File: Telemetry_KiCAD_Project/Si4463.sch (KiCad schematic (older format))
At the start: 16 parts

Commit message: Annotated Components
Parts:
- gave numbers to parts that had none: 16

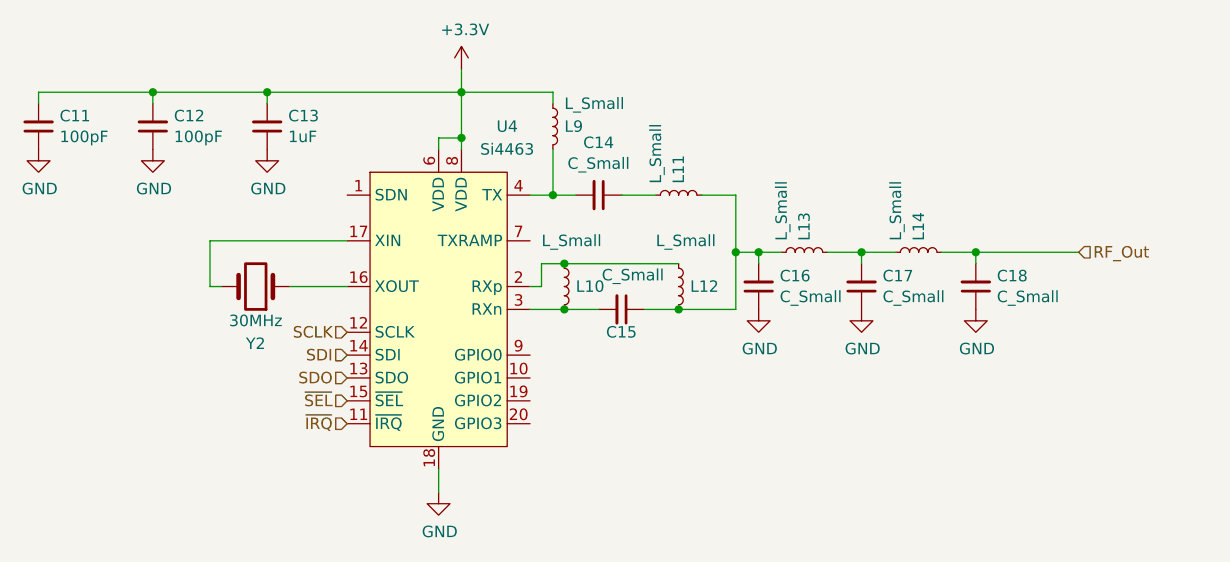
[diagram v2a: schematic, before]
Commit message: Corrected hierarchical pin directions, squashed bugs
There are still some warnings about pins being connected but not driven, don't know how to fix those at the moment
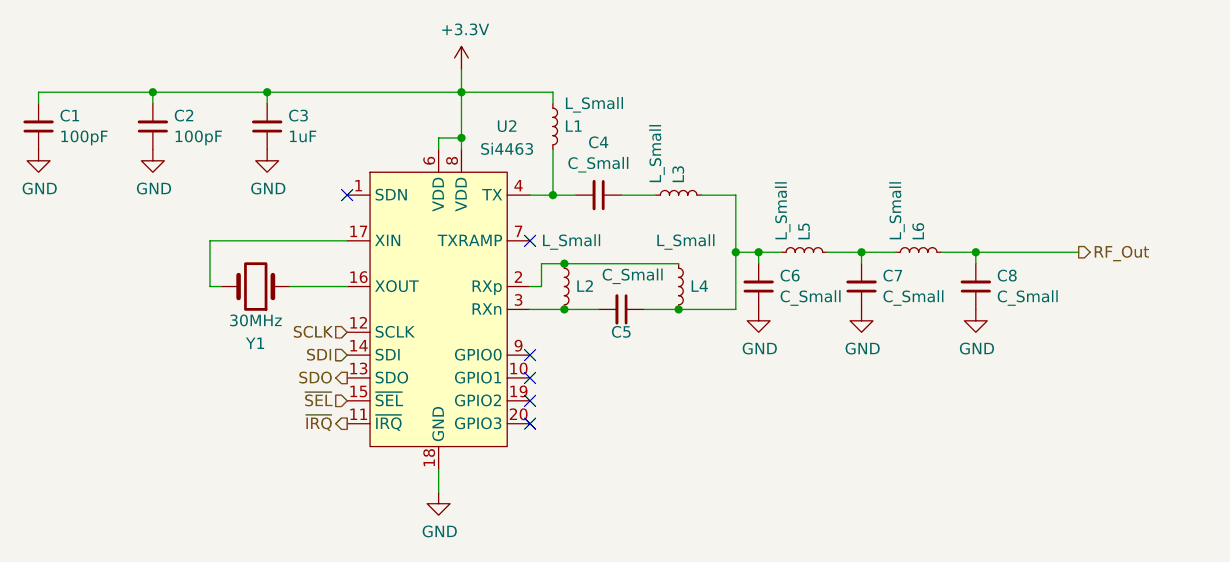
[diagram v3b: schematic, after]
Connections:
- no-connect marks 0 -> 6
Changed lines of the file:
@@
 AR Path="/619D9C89/619D9E16" Ref="U2"  Part="1"
 AR Path="/61A0416A/619D9E16" Ref="U4"  Part="1"
-F 0 "U4" H 6450 4450 50  0000 C CNN
+F 0 "U2" H 6450 4450 50  0000 C CNN
 F 1 "Si4463" H 6450 4350 50  0000 C CNN
 F 2 "Package_DFN_QFN:QFN-20-1EP_4x4mm_P0.5mm_EP2.6x2.6mm_ThermalVias" H 6150 4850 50  0001 C CNN
@@
 AR Path="/619D9C89/619DA640" Ref="C4"  Part="1"
 AR Path="/61A0416A/619DA640" Ref="C14"  Part="1"
-F 0 "C14" V 6621 3150 50  0000 C CNN
+F 0 "C4" V 6621 3150 50  0000 C CNN
 F 1 "C_Small" V 6712 3150 50  0000 C CNN
 F 2 "" H 6850 3150 50  0001 C CNN
@@
 Text HLabel 5750 4050 0    50   Input ~ 0
 ~SEL
-Text HLabel 5750 4150 0    50   Input ~ 0
+Text HLabel 5750 4150 0    50   Output ~ 0
 ~IRQ
-Text HLabel 5750 3950 0    50   Input ~ 0
+Text HLabel 5750 3950 0    50   Output ~ 0
 SDO
 Text HLabel 5750 3850 0    50   Input ~ 0
@@
 AR Path="/619D9C89/619DAC0C" Ref="Y1"  Part="1"
 AR Path="/61A0416A/619DAC0C" Ref="Y2"  Part="1"
-F 0 "Y2" H 5350 3800 50  0000 C CNN
+F 0 "Y1" H 5350 3800 50  0000 C CNN
 F 1 "30MHz" H 5350 3700 50  0000 C CNN
 F 2 "" H 5350 3550 50  0001 C CNN
@@
 AR Path="/619D9C89/619DA828" Ref="L2"  Part="1"
 AR Path="/61A0416A/619DA828" Ref="L10"  Part="1"
-F 0 "L10" H 6750 3550 50  0000 L CNN
+F 0 "L2" H 6750 3550 50  0000 L CNN
 F 1 "L_Small" H 6600 3750 50  0000 L CNN
 F 2 "" H 6700 3550 50  0001 C CNN
@@
 AR Path="/619D9C89/619E6B72" Ref="L3"  Part="1"
 AR Path="/61A0416A/619E6B72" Ref="L11"  Part="1"
-F 0 "L11" H 7250 3150 50  0000 L CNN
+F 0 "L3" H 7250 3150 50  0000 L CNN
 F 1 "L_Small" H 7250 3250 50  0000 L CNN
 F 2 "" H 7200 3150 50  0001 C CNN
@@
 AR Path="/619D9C89/619E8DE5" Ref="C5"  Part="1"
 AR Path="/61A0416A/619E8DE5" Ref="C15"  Part="1"
-F 0 "C15" V 7050 3650 50  0000 C CNN
+F 0 "C5" V 7050 3650 50  0000 C CNN
 F 1 "C_Small" V 6800 3700 50  0000 C CNN
 F 2 "" H 6950 3650 50  0001 C CNN
@@
 AR Path="/619D9C89/619EAA94" Ref="L4"  Part="1"
 AR Path="/61A0416A/619EAA94" Ref="L12"  Part="1"
-F 0 "L12" H 7250 3550 50  0000 L CNN
+F 0 "L4" H 7250 3550 50  0000 L CNN
 F 1 "L_Small" H 7100 3750 50  0000 L CNN
 F 2 "" H 7200 3550 50  0001 C CNN
@@
 AR Path="/619D9C89/619ECD33" Ref="C6"  Part="1"
 AR Path="/61A0416A/619ECD33" Ref="C16"  Part="1"
-F 0 "C16" H 7458 3504 50  0000 R CNN
+F 0 "C6" H 7458 3504 50  0000 R CNN
 F 1 "C_Small" H 7458 3595 50  0000 R CNN
 F 2 "" H 7550 3550 50  0001 C CNN
@@
 AR Path="/619D9C89/619F2EFE" Ref="L1"  Part="1"
 AR Path="/61A0416A/619F2EFE" Ref="L9"  Part="1"
-F 0 "L9" H 6700 2850 50  0000 L CNN
+F 0 "L1" H 6700 2850 50  0000 L CNN
 F 1 "L_Small" H 6700 2950 50  0000 L CNN
 F 2 "" H 6650 2850 50  0001 C CNN
@@
 AR Path="/619D9C89/619EE414" Ref="C8"  Part="1"
 AR Path="/61A0416A/619EE414" Ref="C18"  Part="1"
-F 0 "C18" H 8408 3504 50  0000 R CNN
+F 0 "C8" H 8408 3504 50  0000 R CNN
 F 1 "C_Small" H 8408 3595 50  0000 R CNN
 F 2 "" H 8500 3550 50  0001 C CNN
@@
 AR Path="/619D9C89/619EDC84" Ref="C7"  Part="1"
 AR Path="/61A0416A/619EDC84" Ref="C17"  Part="1"
-F 0 "C17" H 7908 3504 50  0000 R CNN
+F 0 "C7" H 7908 3504 50  0000 R CNN
 F 1 "C_Small" H 7908 3595 50  0000 R CNN
 F 2 "" H 8000 3550 50  0001 C CNN
@@
 AR Path="/619D9C89/619ECA9B" Ref="L6"  Part="1"
 AR Path="/61A0416A/619ECA9B" Ref="L14"  Part="1"
-F 0 "L14" H 8300 3400 50  0000 L CNN
+F 0 "L6" H 8300 3400 50  0000 L CNN
 F 1 "L_Small" H 8300 3500 50  0000 L CNN
 F 2 "" H 8250 3400 50  0001 C CNN
@@
 AR Path="/619D9C89/619EC46A" Ref="L5"  Part="1"
 AR Path="/61A0416A/619EC46A" Ref="L13"  Part="1"
-F 0 "L13" H 7800 3400 50  0000 L CNN
+F 0 "L5" H 7800 3400 50  0000 L CNN
 F 1 "L_Small" H 7800 3500 50  0000 L CNN
 F 2 "" H 7750 3400 50  0001 C CNN
@@
 AR Path="/619D9C89/619F7D57" Ref="C3"  Part="1"
 AR Path="/61A0416A/619F7D57" Ref="C13"  Part="1"
-F 0 "C13" H 5308 2804 50  0000 R CNN
+F 0 "C3" H 5308 2804 50  0000 R CNN
 F 1 "1uF" H 5308 2895 50  0000 R CNN
 F 2 "" H 5400 2850 50  0001 C CNN
@@
 AR Path="/619D9C89/619F860E" Ref="C2"  Part="1"
 AR Path="/61A0416A/619F860E" Ref="C12"  Part="1"
-F 0 "C12" H 4808 2804 50  0000 R CNN
+F 0 "C2" H 4808 2804 50  0000 R CNN
 F 1 "100pF" H 4808 2895 50  0000 R CNN
 F 2 "" H 4900 2850 50  0001 C CNN
@@
 AR Path="/619D9C89/619F8BD8" Ref="C1"  Part="1"
 AR Path="/61A0416A/619F8BD8" Ref="C11"  Part="1"
-F 0 "C11" H 4308 2804 50  0000 R CNN
+F 0 "C1" H 4308 2804 50  0000 R CNN
 F 1 "100pF" H 4308 2895 50  0000 R CNN
 F 2 "" H 4400 2850 50  0001 C CNN
@@
 Wire Wire Line
 	5400 2700 4900 2700
-Text HLabel 8950 3400 2    50   Input ~ 0
+Text HLabel 8950 3400 2    50   Output ~ 0
 RF_Out
+NoConn ~ 6550 3850
+NoConn ~ 6550 3950
+NoConn ~ 6550 4050
+NoConn ~ 6550 4150
+NoConn ~ 6550 3350
+NoConn ~ 5750 3150
 $EndSCHEMATC

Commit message: Assigned footprints to all components (except duplexer)
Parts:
- C1, C2, C3, C4, C5, C6, C7, C8: footprint (none) -> Capacitor_SMD:C_0603_1608Metric
- L1, L2, L3, L4, L5, L6: footprint (none) -> Inductor_SMD:L_0603_1608Metric
- Y1: footprint (none) -> Crystal:Crystal_SMD_0603-2Pin_6.0x3.5mm
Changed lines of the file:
@@
 F 0 "C4" V 6621 3150 50  0000 C CNN
 F 1 "C_Small" V 6712 3150 50  0000 C CNN
-F 2 "" H 6850 3150 50  0001 C CNN
+F 2 "Capacitor_SMD:C_0603_1608Metric" H 6850 3150 50  0001 C CNN
 F 3 "~" H 6850 3150 50  0001 C CNN
 	1    6850 3150
@@
 AR Path="/619D9C89/619DAEC1" Ref="#PWR0104"  Part="1"
 AR Path="/61A0416A/619DAEC1" Ref="#PWR0116"  Part="1"
-F 0 "#PWR0116" H 6150 4200 50  0001 C CNN
+F 0 "#PWR0104" H 6150 4200 50  0001 C CNN
 F 1 "GND" H 6155 4277 50  0000 C CNN
 F 2 "" H 6150 4450 50  0001 C CNN
@@
 AR Path="/619D9C89/619DB460" Ref="#PWR0105"  Part="1"
 AR Path="/61A0416A/619DB460" Ref="#PWR0117"  Part="1"
-F 0 "#PWR0117" H 6250 2450 50  0001 C CNN
+F 0 "#PWR0105" H 6250 2450 50  0001 C CNN
 F 1 "+3.3V" H 6265 2773 50  0000 C CNN
 F 2 "" H 6250 2600 50  0001 C CNN
@@
 F 0 "Y1" H 5350 3800 50  0000 C CNN
 F 1 "30MHz" H 5350 3700 50  0000 C CNN
-F 2 "" H 5350 3550 50  0001 C CNN
+F 2 "Crystal:Crystal_SMD_0603-2Pin_6.0x3.5mm" H 5350 3550 50  0001 C CNN
 F 3 "~" H 5350 3550 50  0001 C CNN
 	1    5350 3550
@@
 F 0 "L2" H 6750 3550 50  0000 L CNN
 F 1 "L_Small" H 6600 3750 50  0000 L CNN
-F 2 "" H 6700 3550 50  0001 C CNN
+F 2 "Inductor_SMD:L_0603_1608Metric" H 6700 3550 50  0001 C CNN
 F 3 "~" H 6700 3550 50  0001 C CNN
 	1    6700 3550
@@
 F 0 "L3" H 7250 3150 50  0000 L CNN
 F 1 "L_Small" H 7250 3250 50  0000 L CNN
-F 2 "" H 7200 3150 50  0001 C CNN
+F 2 "Inductor_SMD:L_0603_1608Metric" H 7200 3150 50  0001 C CNN
 F 3 "~" H 7200 3150 50  0001 C CNN
 	1    7200 3150
@@
 F 0 "C5" V 7050 3650 50  0000 C CNN
 F 1 "C_Small" V 6800 3700 50  0000 C CNN
-F 2 "" H 6950 3650 50  0001 C CNN
+F 2 "Capacitor_SMD:C_0603_1608Metric" H 6950 3650 50  0001 C CNN
 F 3 "~" H 6950 3650 50  0001 C CNN
 	1    6950 3650
@@
 F 0 "L4" H 7250 3550 50  0000 L CNN
 F 1 "L_Small" H 7100 3750 50  0000 L CNN
-F 2 "" H 7200 3550 50  0001 C CNN
+F 2 "Inductor_SMD:L_0603_1608Metric" H 7200 3550 50  0001 C CNN
 F 3 "~" H 7200 3550 50  0001 C CNN
 	1    7200 3550
@@
 F 0 "C6" H 7458 3504 50  0000 R CNN
 F 1 "C_Small" H 7458 3595 50  0000 R CNN
-F 2 "" H 7550 3550 50  0001 C CNN
+F 2 "Capacitor_SMD:C_0603_1608Metric" H 7550 3550 50  0001 C CNN
 F 3 "~" H 7550 3550 50  0001 C CNN
 	1    7550 3550
@@
 AR Path="/619D9C89/619F22FD" Ref="#PWR0106"  Part="1"
 AR Path="/61A0416A/619F22FD" Ref="#PWR0118"  Part="1"
-F 0 "#PWR0118" H 7550 3400 50  0001 C CNN
+F 0 "#PWR0106" H 7550 3400 50  0001 C CNN
 F 1 "GND" H 7555 3477 50  0000 C CNN
 F 2 "" H 7550 3650 50  0001 C CNN
@@
 F 0 "L1" H 6700 2850 50  0000 L CNN
 F 1 "L_Small" H 6700 2950 50  0000 L CNN
-F 2 "" H 6650 2850 50  0001 C CNN
+F 2 "Inductor_SMD:L_0603_1608Metric" H 6650 2850 50  0001 C CNN
 F 3 "~" H 6650 2850 50  0001 C CNN
 	1    6650 2850
@@
 AR Path="/619D9C89/619F1FAB" Ref="#PWR0107"  Part="1"
 AR Path="/61A0416A/619F1FAB" Ref="#PWR0119"  Part="1"
-F 0 "#PWR0119" H 8000 3400 50  0001 C CNN
+F 0 "#PWR0107" H 8000 3400 50  0001 C CNN
 F 1 "GND" H 8005 3477 50  0000 C CNN
 F 2 "" H 8000 3650 50  0001 C CNN
@@
 AR Path="/619D9C89/619F1D65" Ref="#PWR0108"  Part="1"
 AR Path="/61A0416A/619F1D65" Ref="#PWR0120"  Part="1"
-F 0 "#PWR0120" H 8500 3400 50  0001 C CNN
+F 0 "#PWR0108" H 8500 3400 50  0001 C CNN
 F 1 "GND" H 8505 3477 50  0000 C CNN
 F 2 "" H 8500 3650 50  0001 C CNN
@@
 F 0 "C8" H 8408 3504 50  0000 R CNN
 F 1 "C_Small" H 8408 3595 50  0000 R CNN
-F 2 "" H 8500 3550 50  0001 C CNN
+F 2 "Capacitor_SMD:C_0603_1608Metric" H 8500 3550 50  0001 C CNN
 F 3 "~" H 8500 3550 50  0001 C CNN
 	1    8500 3550
@@
 F 0 "C7" H 7908 3504 50  0000 R CNN
 F 1 "C_Small" H 7908 3595 50  0000 R CNN
-F 2 "" H 8000 3550 50  0001 C CNN
+F 2 "Capacitor_SMD:C_0603_1608Metric" H 8000 3550 50  0001 C CNN
 F 3 "~" H 8000 3550 50  0001 C CNN
 	1    8000 3550
@@
 F 0 "L6" H 8300 3400 50  0000 L CNN
 F 1 "L_Small" H 8300 3500 50  0000 L CNN
-F 2 "" H 8250 3400 50  0001 C CNN
+F 2 "Inductor_SMD:L_0603_1608Metric" H 8250 3400 50  0001 C CNN
 F 3 "~" H 8250 3400 50  0001 C CNN
 	1    8250 3400
@@
 F 0 "L5" H 7800 3400 50  0000 L CNN
 F 1 "L_Small" H 7800 3500 50  0000 L CNN
-F 2 "" H 7750 3400 50  0001 C CNN
+F 2 "Inductor_SMD:L_0603_1608Metric" H 7750 3400 50  0001 C CNN
 F 3 "~" H 7750 3400 50  0001 C CNN
 	1    7750 3400
@@
 F 0 "C3" H 5308 2804 50  0000 R CNN
 F 1 "1uF" H 5308 2895 50  0000 R CNN
-F 2 "" H 5400 2850 50  0001 C CNN
+F 2 "Capacitor_SMD:C_0603_1608Metric" H 5400 2850 50  0001 C CNN
 F 3 "~" H 5400 2850 50  0001 C CNN
 	1    5400 2850
@@
 F 0 "C2" H 4808 2804 50  0000 R CNN
 F 1 "100pF" H 4808 2895 50  0000 R CNN
-F 2 "" H 4900 2850 50  0001 C CNN
+F 2 "Capacitor_SMD:C_0603_1608Metric" H 4900 2850 50  0001 C CNN
 F 3 "~" H 4900 2850 50  0001 C CNN
 	1    4900 2850
@@
 F 0 "C1" H 4308 2804 50  0000 R CNN
 F 1 "100pF" H 4308 2895 50  0000 R CNN
-F 2 "" H 4400 2850 50  0001 C CNN
+F 2 "Capacitor_SMD:C_0603_1608Metric" H 4400 2850 50  0001 C CNN
 F 3 "~" H 4400 2850 50  0001 C CNN
 	1    4400 2850
@@
 AR Path="/619D9C89/619F9745" Ref="#PWR0109"  Part="1"
 AR Path="/61A0416A/619F9745" Ref="#PWR0121"  Part="1"
-F 0 "#PWR0121" H 4400 2700 50  0001 C CNN
+F 0 "#PWR0109" H 4400 2700 50  0001 C CNN
 F 1 "GND" H 4405 2777 50  0000 C CNN
 F 2 "" H 4400 2950 50  0001 C CNN
@@
 AR Path="/619D9C89/619F9A7C" Ref="#PWR0110"  Part="1"
 AR Path="/61A0416A/619F9A7C" Ref="#PWR0122"  Part="1"
-F 0 "#PWR0122" H 4900 2700 50  0001 C CNN
+F 0 "#PWR0110" H 4900 2700 50  0001 C CNN
 F 1 "GND" H 4905 2777 50  0000 C CNN
 F 2 "" H 4900 2950 50  0001 C CNN
@@
 AR Path="/619D9C89/619F9CE2" Ref="#PWR0111"  Part="1"
 AR Path="/61A0416A/619F9CE2" Ref="#PWR0123"  Part="1"
-F 0 "#PWR0123" H 5400 2700 50  0001 C CNN
+F 0 "#PWR0111" H 5400 2700 50  0001 C CNN
 F 1 "GND" H 5405 2777 50  0000 C CNN
 F 2 "" H 5400 2950 50  0001 C CNN

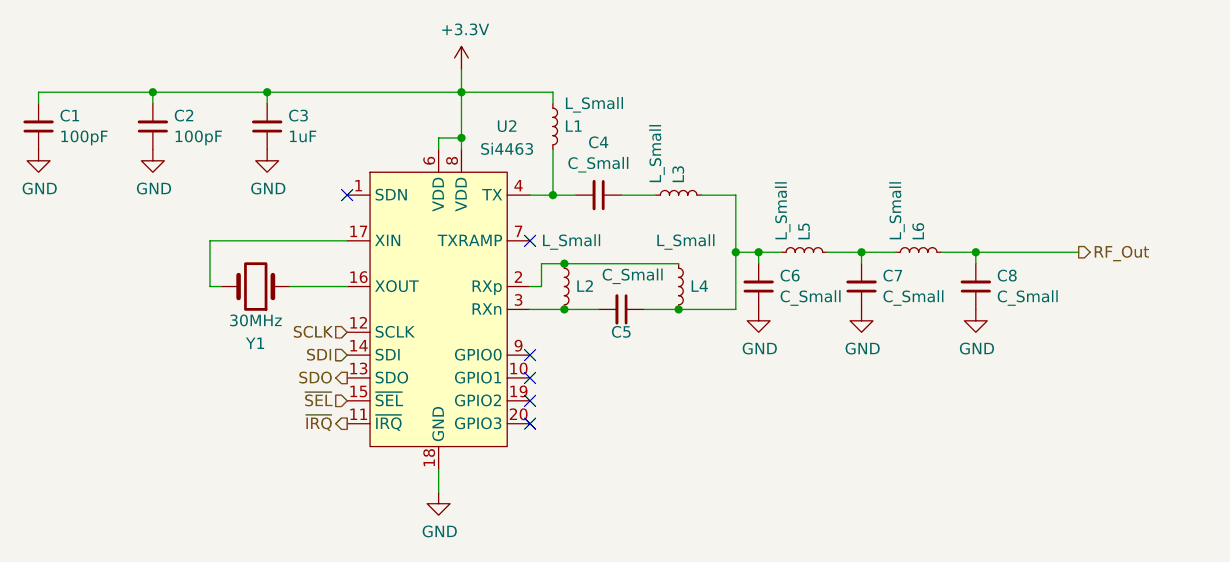
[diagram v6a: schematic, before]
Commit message: Created separate schematics for chips acting in TX and RX
Added link to document describing passive component selection
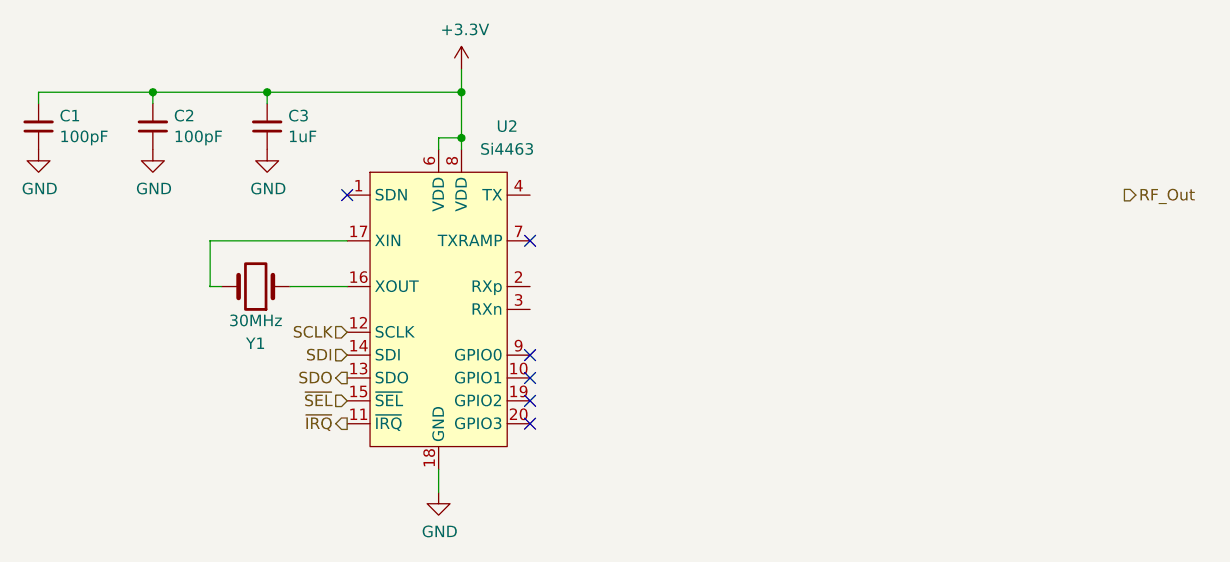
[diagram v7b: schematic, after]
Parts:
- removed C4, C5, C6, C7, C8: C_Small, Capacitor_SMD:C_0603_1608Metric, symbol Device:C_Small
- removed L1, L2, L3, L4, L5, L6: L_Small, Inductor_SMD:L_0603_1608Metric, symbol Device:L_Small
